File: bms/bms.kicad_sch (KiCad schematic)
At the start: 27 parts, among them J1 Conn_01x16_Pin, J10 Conn_01x02_Pin, J11 Conn_01x02_Pin, J12 Conn_01x02_Pin, J13 Conn_01x02_Pin, J14 Conn_01x08_Pin, J15 Conn_01x08_Pin, J16 Conn_01x02_Pin, J17 Conn_01x08_Pin, J18 Conn_01x08_Pin, J19 Conn_01x08_Pin, J2 Conn_01x16_Pin, J20 Conn_01x08_Pin, J21 Conn_01x08_Pin, J22 Conn_01x08_Socket, J23 Conn_01x10_Socket, J24 Conn_01x08_Pin, J25 Conn_01x02_Pin, J26 Conn_01x06_Socket, J27 Conn_01x06_Socket, J3 Conn_01x02_Pin, J4 Conn_01x02_Pin, J5 Conn_01x02_Pin, J6 Conn_01x16_Pin, J7 Conn_01x20_Pin, J8 Conn_01x20_Pin, J9 Conn_01x02_Pin

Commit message: prajeala_maxima_3
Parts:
- removed J1, J2, J6: Conn_01x16_Pin, Connector_PinHeader_2.54mm:PinHeader_2x08_P2.54mm_Vertical, symbol Connector:Conn_01x16_Pin
- removed J7, J8: Conn_01x20_Pin, Connector_PinHeader_2.54mm:PinHeader_2x10_P2.54mm_Vertical, symbol Connector:Conn_01x20_Pin
- added J10, J20, J21: Conn_02x08_Odd_Even, Connector_PinHeader_2.54mm:PinHeader_2x08_P2.54mm_Vertical, symbol Connector_Generic:Conn_02x08_Odd_Even
- added J11, J22: Conn_02x10_Odd_Even, Connector_PinHeader_2.54mm:PinHeader_2x10_P2.54mm_Vertical, symbol Connector_Generic:Conn_02x10_Odd_Even
- renumbered J24 to J1, J19 to J12, J20 to J13, J11 to J14, J13 to J15, J4 to J17, J9 to J18, J10 to J19, J22 to J2, J21 to J23, J3 to J24, J5 to J25, J25 to J26, J12 to J27, J27 to J3, J14 to J4, J23 to J5, J26 to J6, J15 to J7, J17 to J8, J18 to J9
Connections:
- net 1: now also J21.2 (Pin_2)
- net 2: now also J21.4 (Pin_4)
- net 3: now also J21.6 (Pin_6)
- net 4: now also J21.8 (Pin_8)
- net 5: now also J21.10 (Pin_10)
- net 6: now also J21.12 (Pin_12)
- net 7: now also J21.14 (Pin_14)
- net 8: now also J21.16 (Pin_16)
- net Vdd: now also J5.6 (Pin_6), J11.12 (Pin_12); no longer J5.8 (Pin_8)
- net cs: now also J5.2 (Pin_2), J11.18 (Pin_18); no longer J5.4 (Pin_4)
- net miso: now also J5.4 (Pin_4), J11.20 (Pin_20); no longer J5.6 (Pin_6)
- net sck: now also J5.5 (Pin_5), J11.19 (Pin_19); no longer J5.7 (Pin_7)
- net sout: now also J5.3 (Pin_3), J11.17 (Pin_17); no longer J5.5 (Pin_5)
- net at J25.1 (Pin_1): now also J22.12 (Pin_12)
- net at J25.2 (Pin_2): now also J22.10 (Pin_10)
- net at J14.1 (Pin_1): now also J21.5 (Pin_5)
- net at J14.2 (Pin_2): now also J21.7 (Pin_7)
- net at J19.1 (Pin_1): now also J22.17 (Pin_17)
- net at J19.2 (Pin_2): now also J22.19 (Pin_19)
- net at J18.1 (Pin_1): now also J22.13 (Pin_13)
- net at J18.2 (Pin_2): now also J22.15 (Pin_15)
- net at J24.1 (Pin_1): now also J22.4 (Pin_4)
- net at J24.2 (Pin_2): now also J22.2 (Pin_2)
- net at J16.2 (Pin_2): now also J22.3 (Pin_3)
- net at J16.1 (Pin_1): now also J22.1 (Pin_1)
- net at J17.2 (Pin_2): now also J22.7 (Pin_7)
- net at J17.1 (Pin_1): now also J22.5 (Pin_5)
- net at J15.1 (Pin_1): now also J21.9 (Pin_9)
- net at J15.2 (Pin_2): now also J21.11 (Pin_11)
- net Vout+: now reaches J26.2 (Pin_2)
- net Vout+: now also J20.16 (Pin_16)
- net at J5.10 (Pin_10): no longer J26.1 (Pin_1)
- new net GND: J11.10 (Pin_10), J26.1 (Pin_1), J5.8 (Pin_8)
- no-connect marks 26 -> 81
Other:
- note added: "ADBMS6822"
- note added: "Conn_K312-mini J1"
- note added: "Conn_K312-mini J3"
- note added: "Conn_K312-mini J4"
- note added: "Conn_K312-mini J5"
- note added: "Conn_K312-mini J6"
- note added: "Conn_VDD_alim termistori"
- note added: "Conn_alim VCU"
- note added: "K312-mini"
- note added: "SEMNAL TERMISTORI"
- moved on the sheet: J1, J12, J13, J14, J15, J16, J17, J18, J19, J2, J23, J24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

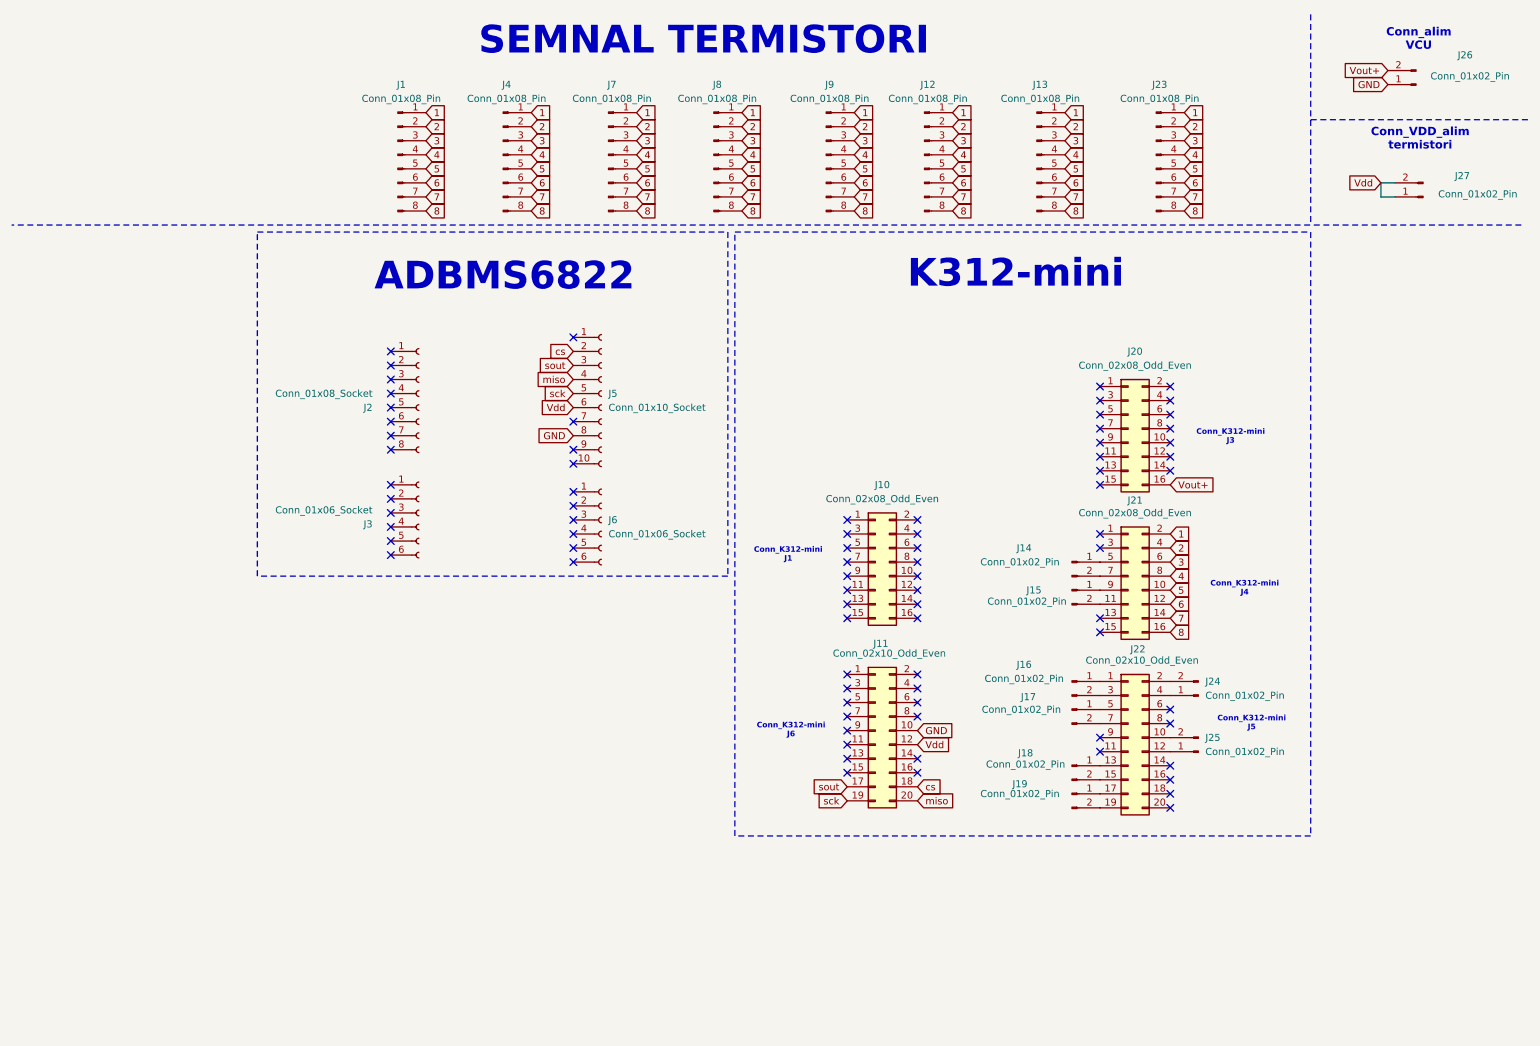
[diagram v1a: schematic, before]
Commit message: idee de pcb bms
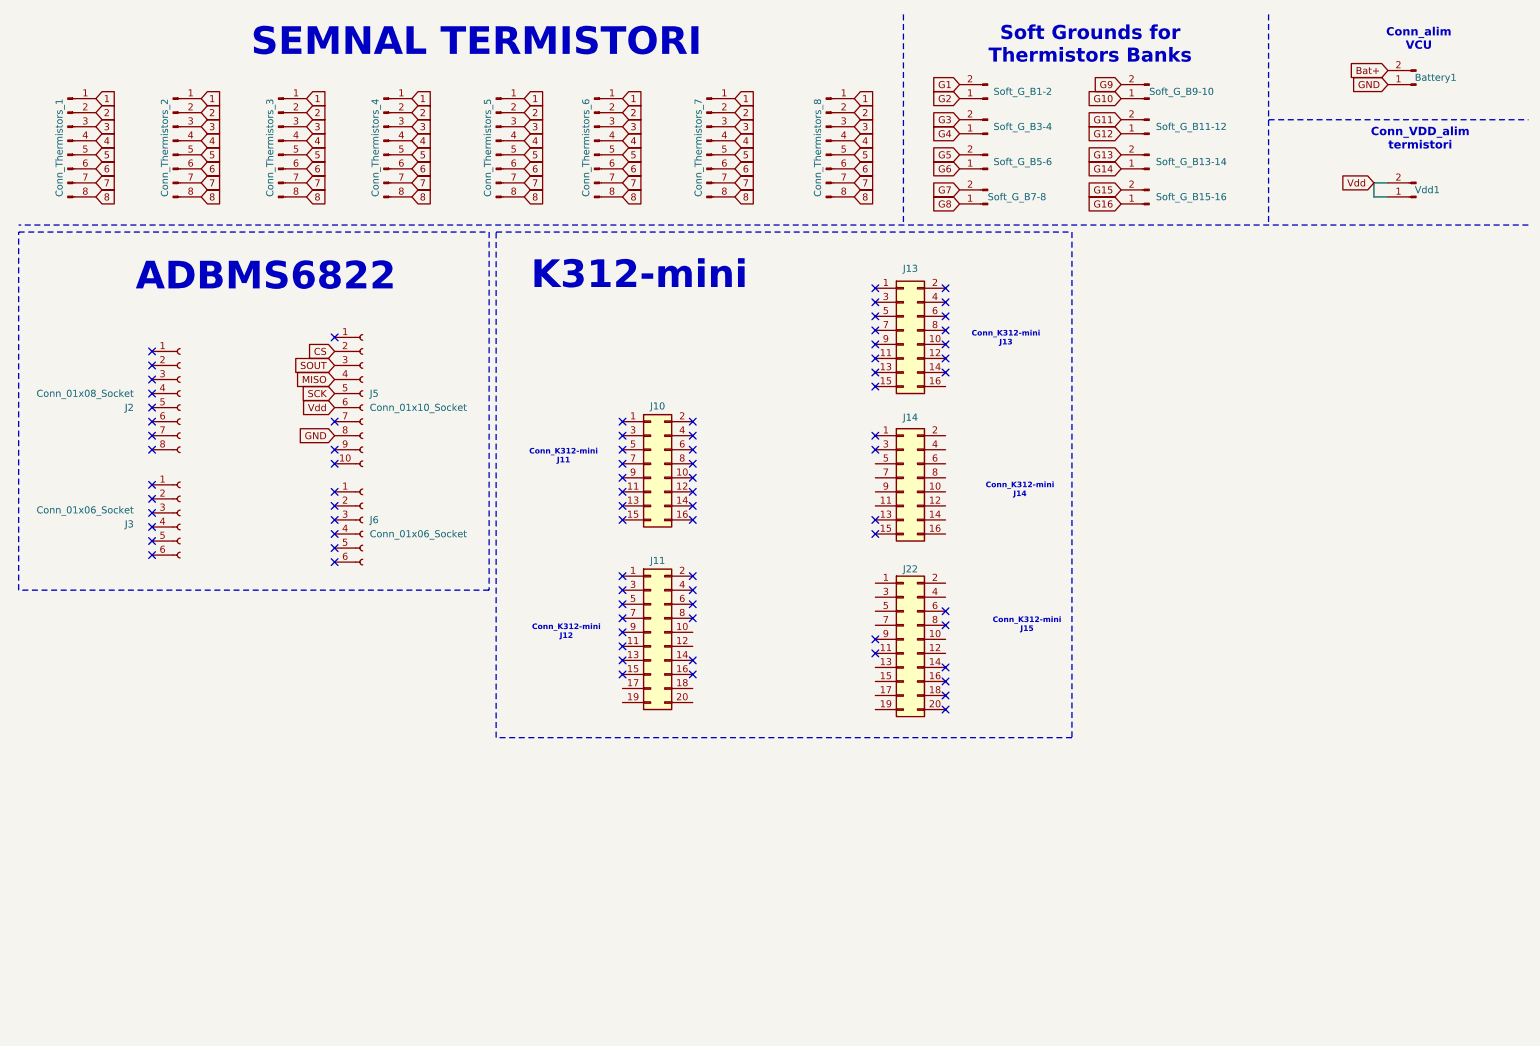
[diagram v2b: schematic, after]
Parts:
- renumbered J26 to Battery1, J1 to Conn_Thermistors_1, J4 to Conn_Thermistors_2, J7 to Conn_Thermistors_3, J8 to Conn_Thermistors_4, J9 to Conn_Thermistors_5, J12 to Conn_Thermistors_6, J13 to Conn_Thermistors_7, J23 to Conn_Thermistors_8, J20 to J13, J21 to J14, J15 to Soft_G_B1-2, J19 to Soft_G_B11-12, J18 to Soft_G_B13-14, J17 to Soft_G_B15-16, J14 to Soft_G_B3-4, J16 to Soft_G_B5-6, J25 to Soft_G_B7-8, J24 to Soft_G_B9-10, J27 to Vdd1
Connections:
- net 1: no longer J14.2 (Pin_2)
- net 2: no longer J14.4 (Pin_4)
- net 3: no longer J14.6 (Pin_6)
- net 4: no longer J14.8 (Pin_8)
- net 5: no longer J14.10 (Pin_10)
- net 6: no longer J14.12 (Pin_12)
- net 7: no longer J14.14 (Pin_14)
- net 8: no longer J14.16 (Pin_16)
- net GND: no longer J11.10 (Pin_10)
- net Vdd: no longer J11.12 (Pin_12)
- net at J22.12 (Pin_12): no longer Soft_G_B7-8.1 (Pin_1)
- net at J22.10 (Pin_10): no longer Soft_G_B7-8.2 (Pin_2)
- net at J14.5 (Pin_5): no longer Soft_G_B3-4.1 (Pin_1)
- net at J14.7 (Pin_7): no longer Soft_G_B3-4.2 (Pin_2)
- net at J22.17 (Pin_17): no longer Soft_G_B11-12.1 (Pin_1)
- net at J22.19 (Pin_19): no longer Soft_G_B11-12.2 (Pin_2)
- net at J14.11 (Pin_11): no longer Soft_G_B1-2.2 (Pin_2)
- net at J14.9 (Pin_9): no longer Soft_G_B1-2.1 (Pin_1)
- net at J22.13 (Pin_13): no longer Soft_G_B13-14.1 (Pin_1)
- net at J22.15 (Pin_15): no longer Soft_G_B13-14.2 (Pin_2)
- net at J22.4 (Pin_4): no longer Soft_G_B9-10.1 (Pin_1)
- net at J22.2 (Pin_2): no longer Soft_G_B9-10.2 (Pin_2)
- net at J22.1 (Pin_1): no longer Soft_G_B5-6.1 (Pin_1)
- net at J22.3 (Pin_3): no longer Soft_G_B5-6.2 (Pin_2)
- net at J22.5 (Pin_5): no longer Soft_G_B15-16.1 (Pin_1)
- net at J22.7 (Pin_7): no longer Soft_G_B15-16.2 (Pin_2)
- net Vout+: no longer names the net of J13.16 (Pin_16)
- net Vout+: no longer Battery1.2 (Pin_2)
- net cs: no longer names the net of J11.18 (Pin_18)
- net cs: no longer J5.2 (Pin_2)
- net miso: no longer names the net of J11.20 (Pin_20)
- net miso: no longer J5.4 (Pin_4)
- net sck: no longer names the net of J11.19 (Pin_19)
- net sck: no longer J5.5 (Pin_5)
- net sout: no longer names the net of J11.17 (Pin_17)
- net sout: no longer J5.3 (Pin_3)
- new net Bat+: Battery1.2 (Pin_2)
- new net CS: J5.2 (Pin_2)
- new net G1: Soft_G_B1-2.2 (Pin_2)
- new net G10: Soft_G_B9-10.1 (Pin_1)
- new net G11: Soft_G_B11-12.2 (Pin_2)
- new net G12: Soft_G_B11-12.1 (Pin_1)
- new net G13: Soft_G_B13-14.2 (Pin_2)
- new net G14: Soft_G_B13-14.1 (Pin_1)
- new net G15: Soft_G_B15-16.2 (Pin_2)
- new net G16: Soft_G_B15-16.1 (Pin_1)
- new net G2: Soft_G_B1-2.1 (Pin_1)
- new net G3: Soft_G_B3-4.2 (Pin_2)
- new net G4: Soft_G_B3-4.1 (Pin_1)
- new net G5: Soft_G_B5-6.2 (Pin_2)
- new net G6: Soft_G_B5-6.1 (Pin_1)
- new net G7: Soft_G_B7-8.2 (Pin_2)
- new net G8: Soft_G_B7-8.1 (Pin_1)
- new net G9: Soft_G_B9-10.2 (Pin_2)
- new net MISO: J5.4 (Pin_4)
- new net SCK: J5.5 (Pin_5)
- new net SOUT: J5.3 (Pin_3)
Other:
- note added: "Conn_K312-mini J11"
- note added: "Conn_K312-mini J12"
- note added: "Conn_K312-mini J13"
- note added: "Conn_K312-mini J14"
- note added: "Conn_K312-mini J15"
- note added: "Soft Grounds for Thermistors Banks"
- note removed: "Conn_K312-mini J1"
- note removed: "Conn_K312-mini J3"
- note removed: "Conn_K312-mini J4"
- note removed: "Conn_K312-mini J5"
- note removed: "Conn_K312-mini J6"
- moved on the sheet: Conn_Thermistors_1, Conn_Thermistors_2, Conn_Thermistors_3, Conn_Thermistors_4, Conn_Thermistors_5, Conn_Thermistors_6, Conn_Thermistors_7, Conn_Thermistors_8, J10, J11, J13, J14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

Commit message: fara program deschis
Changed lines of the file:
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@@
 	(text "K312-mini\n"
 		(exclude_from_sim no)
-		(at 124.968 58.674 0)
+		(at 126.746 58.674 0)
 		(effects
 			(font

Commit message: v0.99
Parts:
- added CAN_Bus_VCU1: Conn_01x02_Pin, Connector_PinHeader_2.00mm:PinHeader_1x02_P2.00mm_Vertical, symbol Connector:Conn_01x02_Pin
- added CAN_IMD1: Conn_01x02_Pin, symbol Connector:Conn_01x02_Pin
- added CAN_k312: Conn_01x02_Pin, Connector_PinHeader_2.54mm:PinHeader_1x02_P2.54mm_Vertical, symbol Connector:Conn_01x02_Pin
- added D1: SS32, Diode_SMD:D_SMB, symbol Diode:SS32
- J6: value Conn_01x06_Socket -> Conn_01x08_Socket; footprint Connector_PinSocket_2.54mm:PinSocket_1x06_P2.54mm_Vertical -> Connector_PinSocket_2.54mm:PinSocket_1x08_P2.54mm_Vertical; symbol Connector:Conn_01x06_Socket -> Connector:Conn_01x08_Socket
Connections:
- net 1: now also J14.1 (Pin_1)
- net 2: now also J14.3 (Pin_3)
- net 3: now also J14.5 (Pin_5)
- net 4: now also J14.7 (Pin_7)
- net 5: now also J14.9 (Pin_9)
- net 6: now also J14.11 (Pin_11)
- net 7: now also J14.13 (Pin_13)
- net 8: now also J14.15 (Pin_15)
- net Bat+: now also J13.1 (Pin_1), D1.1 (K)
- net G1: now also J13.2 (Pin_2)
- net G10: now also J14.4 (Pin_4)
- net G11: now also J14.6 (Pin_6)
- net G12: now also J14.8 (Pin_8)
- net G13: now also J14.10 (Pin_10)
- net G14: now also J14.12 (Pin_12)
- net G15: now also J14.14 (Pin_14)
- net G16: now also J14.16 (Pin_16)
- net G2: now also J13.4 (Pin_4)
- net G3: now also J13.6 (Pin_6)
- net G4: now also J13.8 (Pin_8)
- net G5: now also J13.10 (Pin_10)
- net G6: now also J13.12 (Pin_12)
- net G7: now also J13.14 (Pin_14)
- net G8: now also J13.16 (Pin_16)
- net G9: now also J14.2 (Pin_2)
- net GND: now also J13.13 (Pin_13), D1.2 (A)
- net Vdd: now also J13.9 (Pin_9)
- new net CAN_H_k: CAN_Bus_VCU1.2 (Pin_2), CAN_k312.2 (Pin_2)
- new net CAN_L_k: CAN_Bus_VCU1.1 (Pin_1), CAN_k312.1 (Pin_1)
- no-connect marks 81 -> 89
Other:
- note added: "Conn_CAN"
- moved on the sheet: J2, J3

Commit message: V0.999 a little more polished
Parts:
- added J10: Conn_02x10_Odd_Even, Connector_PinHeader_2.54mm:PinHeader_2x10_P2.54mm_Vertical, symbol Connector_Generic:Conn_02x10_Odd_Even
- CAN_IMD1: now not fitted; now left out of the parts list
- renumbered J10 to J11, J11 to J12, J22 to J15
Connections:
- net CS: now also J10.11 (Pin_11)
- net MISO: now also J10.7 (Pin_7)
- net SCK: now also J10.5 (Pin_5)
- net SOUT: now also J10.9 (Pin_9)
- no-connect marks 89 -> 105
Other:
- moved on the sheet: J11, J12, J13, J14, J15

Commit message: inca un update
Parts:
- CAN_Bus_VCU1: footprint Connector_PinHeader_2.00mm:PinHeader_1x02_P2.00mm_Vertical -> Connector_JST:JST_PH_S2B-PH-K_1x02_P2.00mm_Horizontal
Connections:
- net CAN_H_k: now also CAN_Bus_VCU1.1 (Pin_1); no longer CAN_Bus_VCU1.2 (Pin_2)
- net CAN_L_k: now also CAN_Bus_VCU1.2 (Pin_2); no longer CAN_Bus_VCU1.1 (Pin_1)
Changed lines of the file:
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@@
 		)
 	)
-	(global_label "CAN_H_k"
-		(shape input)
-		(at 260.35 71.12 180)
-		(fields_autoplaced yes)
-		(effects
-			(font
-				(size 1.27 1.27)
-			)
-			(justify right)
-		)
-		(property "Intersheetrefs" "${INTERSHEET_REFS}"
-			(at 249.3819 71.12 0)
-			(effects
-				(font
-					(size 1.27 1.27)
-				)
-				(justify right)
-				(hide yes)
-			)
-		)
-	)
 	(global_label "CAN_L_k"
 		(shape input)
@@
 		)
 	)
+	(global_label "CAN_H_k"
+		(shape input)
+		(at 260.35 73.66 180)
+		(fields_autoplaced yes)
+		(effects
+			(font
+				(size 1.27 1.27)
+			)
+			(justify right)
+		)
+		(property "Intersheetrefs" "${INTERSHEET_REFS}"
+			(at 249.3819 73.66 0)
+			(effects
+				(font
+					(size 1.27 1.27)
+				)
+				(justify right)
+				(hide yes)
+			)
+		)
+	)
 	(global_label "4"
 		(shape input)
@@
 		)
 	)
+	(global_label "CAN_L_k"
+		(shape input)
+		(at 260.35 71.12 180)
+		(fields_autoplaced yes)
+		(effects
+			(font
+				(size 1.27 1.27)
+			)
+			(justify right)
+		)
+		(property "Intersheetrefs" "${INTERSHEET_REFS}"
+			(at 249.6843 71.12 0)
+			(effects
+				(font
+					(size 1.27 1.27)
+				)
+				(justify right)
+				(hide yes)
+			)
+		)
+	)
 	(global_label "3"
 		(shape input)
@@
 		)
 	)
-	(global_label "CAN_L_k"
-		(shape input)
-		(at 260.35 73.66 180)
-		(fields_autoplaced yes)
-		(effects
-			(font
-				(size 1.27 1.27)
-			)
-			(justify right)
-		)
-		(property "Intersheetrefs" "${INTERSHEET_REFS}"
-			(at 249.6843 73.66 0)
-			(effects
-				(font
-					(size 1.27 1.27)
-				)
-				(justify right)
-				(hide yes)
-			)
-		)
-	)
 	(global_label "G9"
 		(shape input)
@@
 			)
 		)
-		(property "Footprint" "Connector_PinHeader_2.00mm:PinHeader_1x02_P2.00mm_Vertical"
+		(property "Footprint" "Connector_JST:JST_PH_S2B-PH-K_1x02_P2.00mm_Horizontal"
 			(at 265.43 73.66 0)
 			(effects
